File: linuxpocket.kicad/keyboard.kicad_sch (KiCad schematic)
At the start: 4 parts, among them U7 BBQ10KBD, U8 ATmega32U4-M

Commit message: Keyboard done. (Except mic) #2
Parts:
- added C22: 1uF, Capacitor_SMD:C_0402_1005Metric, symbol Device:C
- added C23, C24, C25: 47nF, symbol Device:C
- added Q1: MMBT3904, Package_TO_SOT_SMD:SOT-23, symbol Transistor_BJT:MMBT3904
- added TP1, TP2, TP3, TP4: TestPoint, symbol Connector:TestPoint
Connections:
- net +3V3: now also U7.2 (MIC_VDD), U8.42 (AREF), U8.6 (UCAP), C22.1, C23.2, C24.1
- net GND: now also C22.2, C23.1, C24.2, C25.2, Q1.2 (E)
- net MOSI: now reaches U7.10 (COL3), U8.10 (PB2)
- net MOSI: now also TP3.1
- net MISO: now reaches U7.17 (COL4), U8.11 (PB3)
- net MISO: now also TP4.1
- net at U7.23 (LEDK_2_3): now also U7.25 (LEDK_1_4), Q1.3 (C)
- net SCK: now reaches U7.9 (COL2), U8.9 (PB1)
- net SCK: now also TP2.1
- net RESET: now reaches U8.13 (~{RESET})
- net RESET: now also TP1.1
- net +5V: now reaches U8.2 (UVCC)
- net +5V: now also U8.7 (VBUS), C25.1
- net at U8.27 (PD7): now also Q1.1 (B)
- no-connect marks 0 -> 2
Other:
- note added: "CHECK MICVDD"
- note added: "Decoupling capacitors"
- note added: "Place close to IC"
- note added: "Programming ISP"
- moved on the sheet: R22, R23, U7, U8

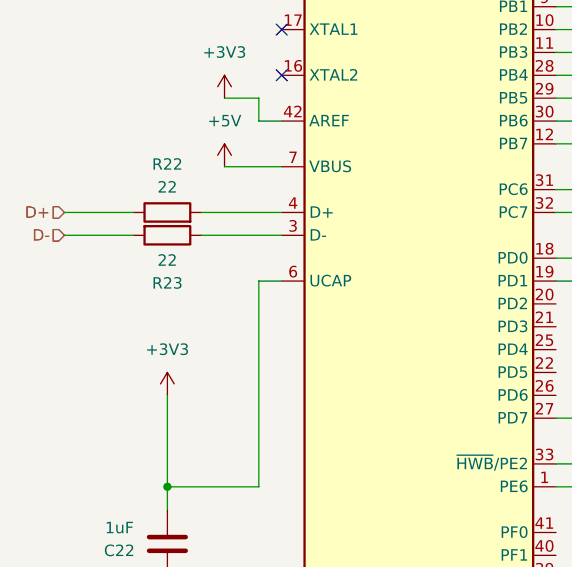
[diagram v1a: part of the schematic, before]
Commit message: Add magnetometer #5. Add footprints to some symbols.
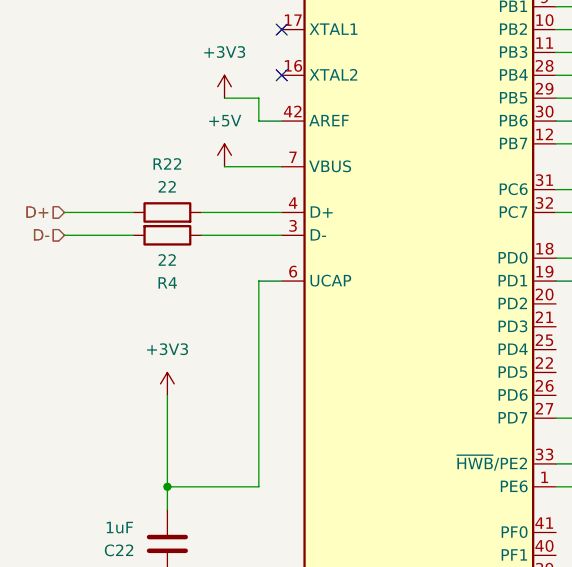
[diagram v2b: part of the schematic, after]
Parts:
- removed R23: 22, symbol Device:R
- added R4: 22, Resistor_SMD:R_0402_1005Metric, symbol Device:R
- C23, C24, C25: footprint (none) -> Capacitor_SMD:C_0603_1608Metric; LCSC (none) -> C1622
- R22: footprint (none) -> Resistor_SMD:R_0402_1005Metric; LCSC (none) -> C25092
- TP1, TP2, TP3, TP4: footprint (none) -> TestPoint:TestPoint_THTPad_D1.0mm_Drill0.5mm
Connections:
- net +3V3: now also C23.1; no longer C23.2
- net D-: now also R4.2
- net GND: now also C23.2; no longer C23.1
- net at U8.3 (D-): now also R4.1

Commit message: PCB almost done and schematic finished.
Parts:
- removed TP2, TP3, TP4: TestPoint, TestPoint:TestPoint_THTPad_D1.0mm_Drill0.5mm, symbol Connector:TestPoint
- added MI1, MO1, SCK1: TestPoint, TestPoint:TestPoint_Pad_D1.0mm, symbol Connector:TestPoint
- RST1: renamed from TP1; footprint TestPoint:TestPoint_THTPad_D1.0mm_Drill0.5mm -> TestPoint:TestPoint_Pad_D1.0mm
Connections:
- net MISO: now also MI1.1; no longer U7.17 (COL4)
- net MOSI: now also MO1.1; no longer U7.10 (COL3)
- net SCK: now also SCK1.1; no longer U7.9 (COL2)
- net VOL_DOWN: now also U8.18 (PD0); no longer U8.1 (PE6)
- net at U7.18 (ROW3): now also U8.26 (PD6); no longer U8.12 (PB7)
- net at U7.19 (COL5): now also U8.27 (PD7); no longer U8.28 (PB4)
- net at U7.20 (ROW4): now also U8.28 (PB4); no longer U8.31 (PC6)
- net at U7.21 (ROW5): now also U8.29 (PB5); no longer U8.32 (PC7)
- net at U7.22 (ROW6): now also U8.30 (PB6); no longer U8.18 (PD0)
- net at U7.27 (ROW7): now also U8.31 (PC6); no longer U8.19 (PD1)
- net at U7.6 (ROW1): now also U8.36 (PF7); no longer U8.29 (PB5)
- net at U7.7 (COL1): now also U8.37 (PF6); no longer U8.8 (PB0)
- net at U7.8 (ROW2): now also U8.38 (PF5); no longer U8.30 (PB6)
- net at Q1.1 (B): now also U8.1 (PE6); no longer U8.27 (PD7)
- net at U8.25 (PD4): now also U7.17 (COL4)
- net at U8.39 (PF4): now also U7.9 (COL2)
- net at U8.40 (PF1): now also U7.10 (COL3)
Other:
- moved on the sheet: Q1, U7
